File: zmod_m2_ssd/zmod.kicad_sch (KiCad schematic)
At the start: 16 parts, among them J1 MDT420M02001, J2 QTH-020-01-X-D-DP-A, U1 SN74LVC1T45DBV

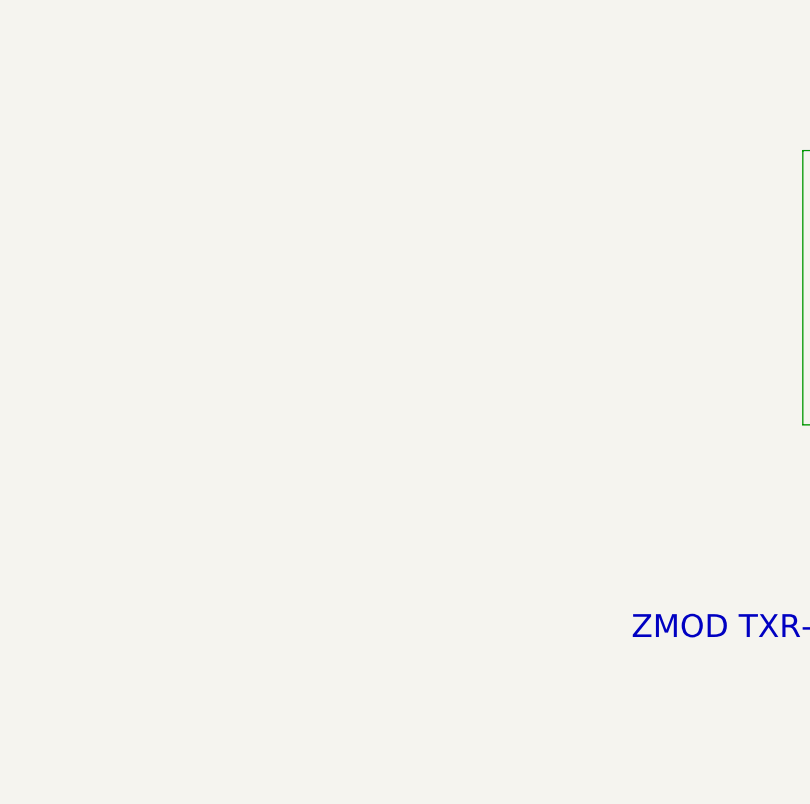
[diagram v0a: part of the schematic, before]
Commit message: adding clock chips for M.2
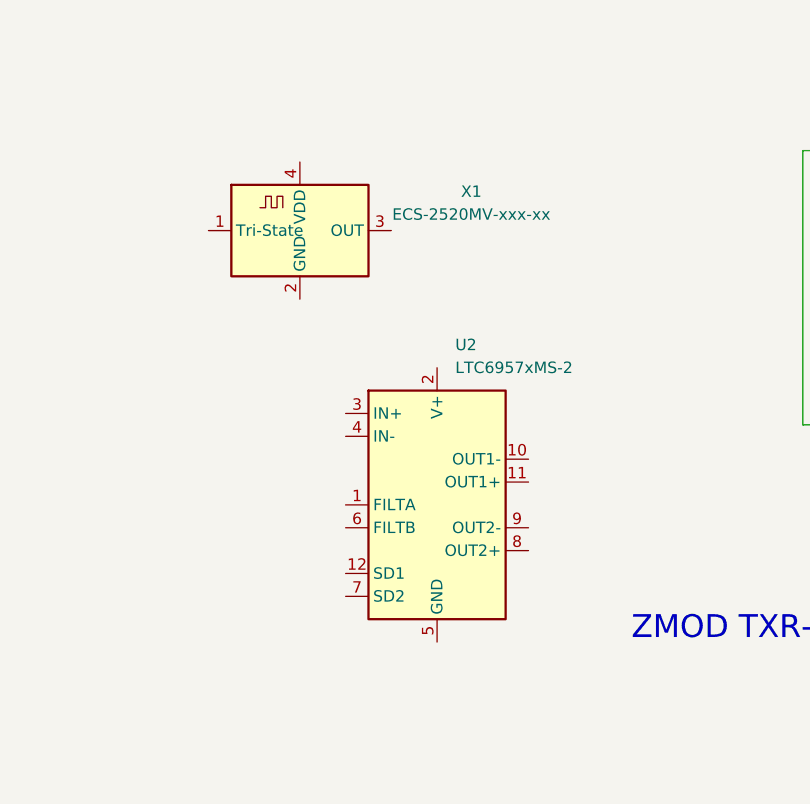
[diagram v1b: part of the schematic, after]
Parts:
- added U2: LTC6957xMS-2, Package_SO:MSOP-12_3x4mm_P0.65mm, symbol Interface:LTC6957xMS-2
- added X1: ECS-2520MV-xxx-xx, Oscillator:Oscillator_SMD_ECS_2520MV-xxx-xx-4Pin_2.5x2.0mm, symbol Oscillator:ECS-2520MV-xxx-xx
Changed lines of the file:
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@@
     (pin "9")
   )
-  (symbol (lib_id "power:+5V") (at 83.82 57.15 0) (unit 1)
-    (in_bom yes) (on_board yes) (fields_autoplaced)
-    (property "Reference" "#PWR02" (id 0) (at 83.82 60.96 0)
-      (effects (font (size 1.27 1.27)) hide)
-    )
-    (property "Value" "+5V" (id 1) (at 83.82 52.07 0))
-    (property "Footprint" "" (id 2) (at 83.82 57.15 0)
-      (effects (font (size 1.27 1.27)) hide)
-    )
-    (property "Datasheet" "" (id 3) (at 83.82 57.15 0)
-      (effects (font (size 1.27 1.27)) hide)
-    )
-    (pin "1")
-  )
-  (symbol (lib_id "power:+3V3") (at 269.24 72.39 0) (unit 1)
-    (in_bom yes) (on_board yes)
-    (property "Reference" "#PWR010" (id 0) (at 269.24 76.2 0)
-      (effects (font (size 1.27 1.27)) hide)
-    )
-    (property "Value" "+3V3" (id 1) (at 270.51 71.12 0)
-      (effects (font (size 1.27 1.27)) (justify left))
-    )
-    (property "Footprint" "" (id 2) (at 269.24 72.39 0)
-      (effects (font (size 1.27 1.27)) hide)
-    )
-    (property "Datasheet" "" (id 3) (at 269.24 72.39 0)
-      (effects (font (size 1.27 1.27)) hide)
-    )
-    (pin "1")
-  )
-  (symbol (lib_id "power:GND") (at 82.55 146.05 0) (unit 1)
-    (in_bom yes) (on_board yes) (fields_autoplaced)
-    (property "Reference" "#PWR0101" (id 0) (at 82.55 152.4 0)
-      (effects (font (size 1.27 1.27)) hide)
-    )
-    (property "Value" "GND" (id 1) (at 82.55 151.13 0))
-    (property "Footprint" "" (id 2) (at 82.55 146.05 0)
-      (effects (font (size 1.27 1.27)) hide)
-    )
-    (property "Datasheet" "" (id 3) (at 82.55 146.05 0)
-      (effects (font (size 1.27 1.27)) hide)
-    )
-    (pin "1")
-  )
-  (symbol (lib_id "Mechanical:MountingHole_Pad") (at 38.1 191.77 0) (unit 1)
-    (in_bom yes) (on_board yes) (fields_autoplaced)
-    (property "Reference" "H3" (id 0) (at 40.64 189.2299 0)
-      (effects (font (size 1.27 1.27)) (justify left))
-    )
-    (property "Value" "MountingHole_Pad" (id 1) (at 40.64 191.7699 0)
-      (effects (font (size 1.27 1.27)) (justify left) hide)
-    )
-    (property "Footprint" "MountingHole:MountingHole_3.2mm_M3_DIN965_Pad_TopBottom" (id 2) (at 38.1 191.77 0)
-      (effects (font (size 1.27 1.27)) hide)
-    )
-    (property "Datasheet" "~" (id 3) (at 38.1 191.77 0)
-      (effects (font (size 1.27 1.27)) hide)
-    )
-    (pin "1")
-  )
-  (symbol (lib_id "Logic_LevelTranslator:SN74LVC1T45DBV") (at 146.05 50.8 0) (mirror y) (unit 1)
-    (in_bom yes) (on_board yes) (fields_autoplaced)
-    (property "Reference" "U1" (id 0) (at 128.27 46.4693 0))
-    (property "Value" "SN74LVC1T45DBV" (id 1) (at 128.27 49.0093 0))
-    (property "Footprint" "Package_TO_SOT_SMD:SOT-23-6" (id 2) (at 146.05 62.23 0)
-      (effects (font (size 1.27 1.27)) hide)
-    )
-    (property "Datasheet" "http://www.ti.com/lit/ds/symlink/sn74lvc1t45.pdf" (id 3) (at 168.91 67.31 0)
-      (effects (font (size 1.27 1.27)) hide)
-    )
-    (pin "1")
+  (symbol (lib_id "Interface:LTC6957xMS-2") (at 162.56 156.21 0) (unit 1)
+    (in_bom yes) (on_board yes) (fields_autoplaced)
+    (property "Reference" "U2" (id 0) (at 164.5794 138.43 0)
+      (effects (font (size 1.27 1.27)) (justify left))
+    )
+    (property "Value" "LTC6957xMS-2" (id 1) (at 164.5794 140.97 0)
+      (effects (font (size 1.27 1.27)) (justify left))
+    )
+    (property "Footprint" "Package_SO:MSOP-12_3x4mm_P0.65mm" (id 2) (at 162.56 172.72 0)
+      (effects (font (size 1.27 1.27)) hide)
+    )
+    (property "Datasheet" "https://www.analog.com/media/en/technical-documentation/data-sheets/6957fb.pdf" (id 3) (at 162.56 156.21 0)
+      (effects (font (size 1.27 1.27)) hide)
+    )
+    (pin "1")
+    (pin "10")
+    (pin "11")
+    (pin "12")
     (pin "2")
     (pin "3")
@@
     (pin "5")
     (pin "6")
+    (pin "7")
+    (pin "8")
+    (pin "9")
+  )
+  (symbol (lib_id "power:+5V") (at 83.82 57.15 0) (unit 1)
+    (in_bom yes) (on_board yes) (fields_autoplaced)
+    (property "Reference" "#PWR02" (id 0) (at 83.82 60.96 0)
+      (effects (font (size 1.27 1.27)) hide)
+    )
+    (property "Value" "+5V" (id 1) (at 83.82 52.07 0))
+    (property "Footprint" "" (id 2) (at 83.82 57.15 0)
+      (effects (font (size 1.27 1.27)) hide)
+    )
+    (property "Datasheet" "" (id 3) (at 83.82 57.15 0)
+      (effects (font (size 1.27 1.27)) hide)
+    )
+    (pin "1")
+  )
+  (symbol (lib_id "Oscillator:ECS-2520MV-xxx-xx") (at 147.32 125.73 0) (unit 1)
+    (in_bom yes) (on_board yes) (fields_autoplaced)
+    (property "Reference" "X1" (id 0) (at 166.37 121.3993 0))
+    (property "Value" "ECS-2520MV-xxx-xx" (id 1) (at 166.37 123.9393 0))
+    (property "Footprint" "Oscillator:Oscillator_SMD_ECS_2520MV-xxx-xx-4Pin_2.5x2.0mm" (id 2) (at 158.75 134.62 0)
+      (effects (font (size 1.27 1.27)) hide)
+    )
+    (property "Datasheet" "https://www.ecsxtal.com/store/pdf/ECS-2520MV.pdf" (id 3) (at 142.875 122.555 0)
+      (effects (font (size 1.27 1.27)) hide)
+    )
+    (pin "1")
+    (pin "2")
+    (pin "3")
+    (pin "4")
+  )
+  (symbol (lib_id "power:+3V3") (at 269.24 72.39 0) (unit 1)
+    (in_bom yes) (on_board yes)
+    (property "Reference" "#PWR010" (id 0) (at 269.24 76.2 0)
+      (effects (font (size 1.27 1.27)) hide)
+    )
+    (property "Value" "+3V3" (id 1) (at 270.51 71.12 0)
+      (effects (font (size 1.27 1.27)) (justify left))
+    )
+    (property "Footprint" "" (id 2) (at 269.24 72.39 0)
+      (effects (font (size 1.27 1.27)) hide)
+    )
+    (property "Datasheet" "" (id 3) (at 269.24 72.39 0)
+      (effects (font (size 1.27 1.27)) hide)
+    )
+    (pin "1")
+  )
+  (symbol (lib_id "power:GND") (at 82.55 146.05 0) (unit 1)
+    (in_bom yes) (on_board yes) (fields_autoplaced)
+    (property "Reference" "#PWR0101" (id 0) (at 82.55 152.4 0)
+      (effects (font (size 1.27 1.27)) hide)
+    )
+    (property "Value" "GND" (id 1) (at 82.55 151.13 0))
+    (property "Footprint" "" (id 2) (at 82.55 146.05 0)
+      (effects (font (size 1.27 1.27)) hide)
+    )
+    (property "Datasheet" "" (id 3) (at 82.55 146.05 0)
+      (effects (font (size 1.27 1.27)) hide)
+    )
+    (pin "1")
+  )
+  (symbol (lib_id "Mechanical:MountingHole_Pad") (at 38.1 191.77 0) (unit 1)
+    (in_bom yes) (on_board yes) (fields_autoplaced)
+    (property "Reference" "H3" (id 0) (at 40.64 189.2299 0)
+      (effects (font (size 1.27 1.27)) (justify left))
+    )
+    (property "Value" "MountingHole_Pad" (id 1) (at 40.64 191.7699 0)
+      (effects (font (size 1.27 1.27)) (justify left) hide)
+    )
+    (property "Footprint" "MountingHole:MountingHole_3.2mm_M3_DIN965_Pad_TopBottom" (id 2) (at 38.1 191.77 0)
+      (effects (font (size 1.27 1.27)) hide)
+    )
+    (property "Datasheet" "~" (id 3) (at 38.1 191.77 0)
+      (effects (font (size 1.27 1.27)) hide)
+    )
+    (pin "1")
+  )
+  (symbol (lib_id "Logic_LevelTranslator:SN74LVC1T45DBV") (at 146.05 50.8 0) (mirror y) (unit 1)
+    (in_bom yes) (on_board yes) (fields_autoplaced)
+    (property "Reference" "U1" (id 0) (at 128.27 46.4693 0))
+    (property "Value" "SN74LVC1T45DBV" (id 1) (at 128.27 49.0093 0))
+    (property "Footprint" "Package_TO_SOT_SMD:SOT-23-6" (id 2) (at 146.05 62.23 0)
+      (effects (font (size 1.27 1.27)) hide)
+    )
+    (property "Datasheet" "http://www.ti.com/lit/ds/symlink/sn74lvc1t45.pdf" (id 3) (at 168.91 67.31 0)
+      (effects (font (size 1.27 1.27)) hide)
+    )
+    (pin "1")
+    (pin "2")
+    (pin "3")
+    (pin "4")
+    (pin "5")
+    (pin "6")
   )
   (symbol (lib_id "power:GND") (at 238.76 151.13 0) (unit 1)
@@
       (reference "U1") (unit 1) (value "SN74LVC1T45DBV") (footprint "Package_TO_SOT_SMD:SOT-23-6")
     )
-  )
+    (path "/73d9a73e-e38d-4675-ba62-7d628305395e"
+      (reference "U2") (unit 1) (value "LTC6957xMS-2") (footprint "Package_SO:MSOP-12_3x4mm_P0.65mm")
+    )
+    (path "/7c512e96-8c27-4e61-97e0-2f602c82f7f4"
+      (reference "X1") (unit 1) (value "ECS-2520MV-xxx-xx") (footprint "Oscillator:Oscillator_SMD_ECS_2520MV-xxx-xx-4Pin_2.5x2.0mm")
+    )
+  )

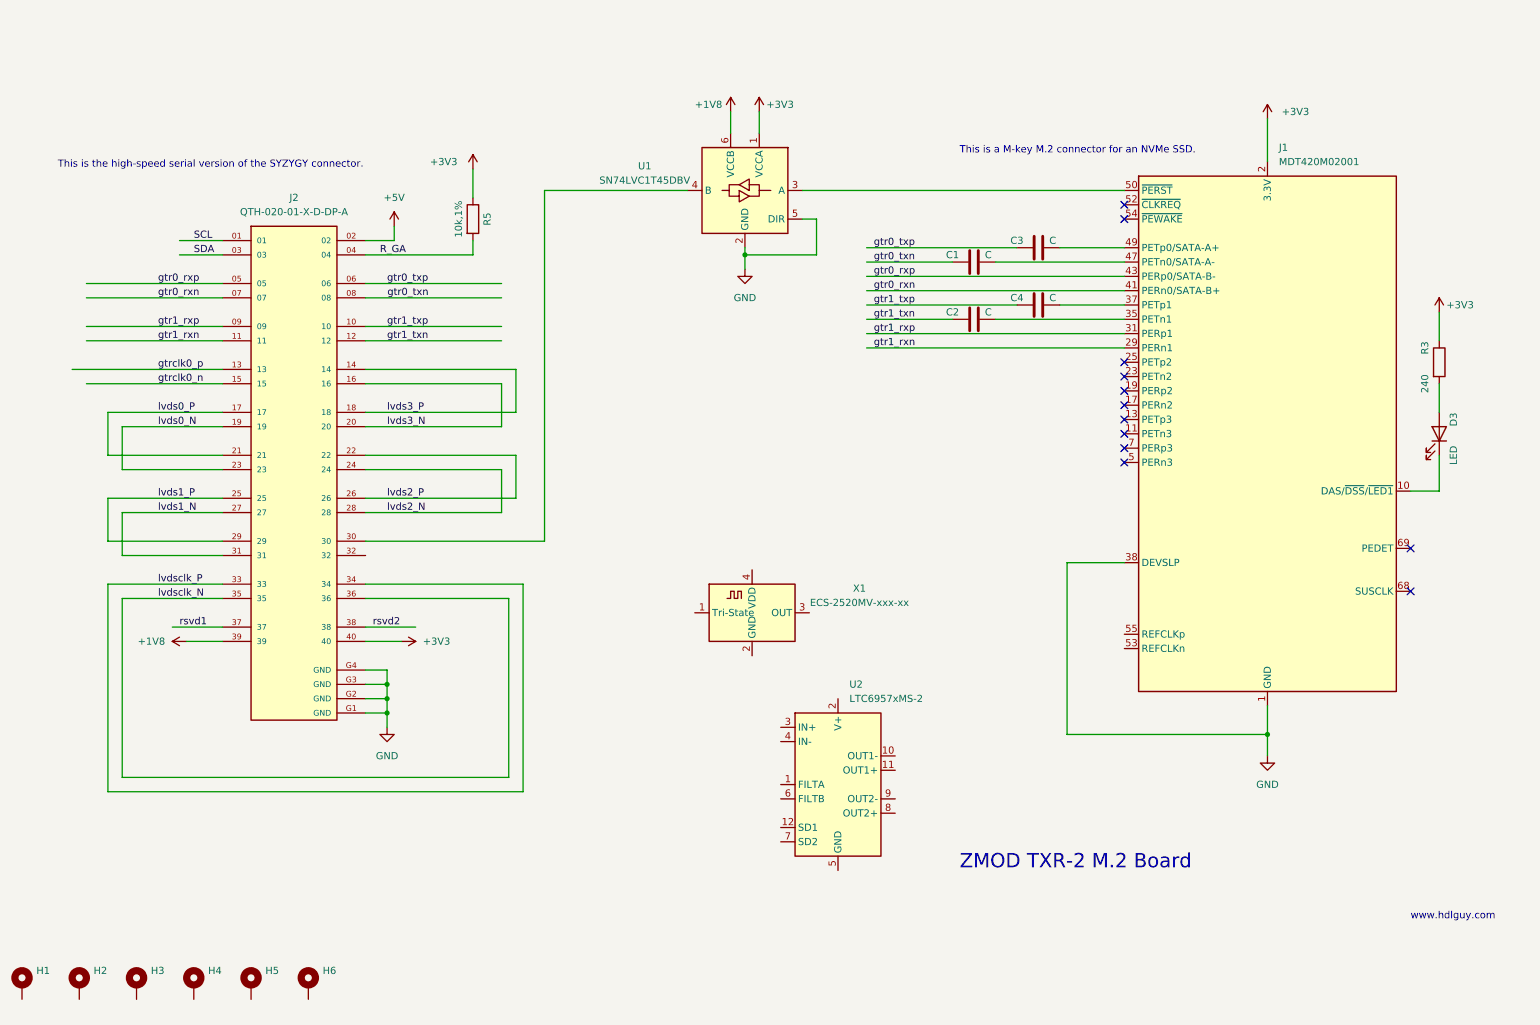
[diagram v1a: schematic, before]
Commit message: added referenc oscillator and clock buffer.
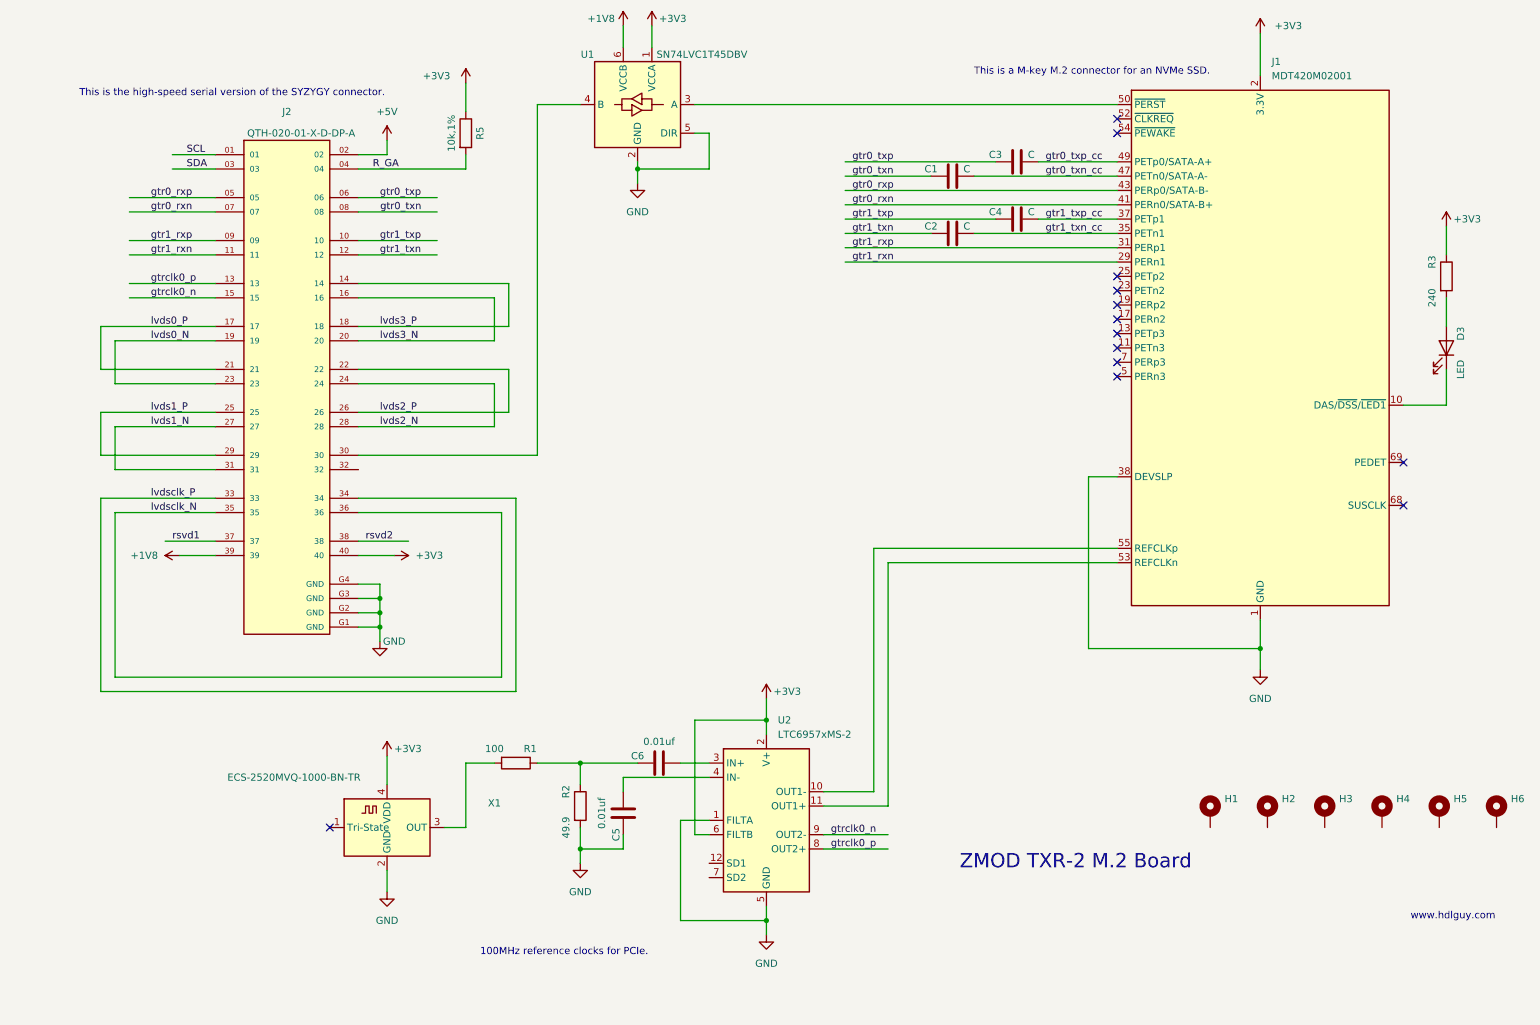
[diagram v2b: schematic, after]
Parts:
- added C5, C6: 0.01uf, Capacitor_SMD:C_0603_1608Metric, symbol Device:C
- added R1: 100, Resistor_SMD:R_0603_1608Metric, symbol Device:R
- added R2: 49.9, Resistor_SMD:R_0603_1608Metric, symbol Device:R
- X1: value ECS-2520MV-xxx-xx -> ECS-2520MVQ-1000-BN-TR
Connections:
- net +3V3: now also U2.2 (V+), U2.6 (FILTB), X1.4 (VDD)
- net GND: now also U2.1 (FILTA), U2.5 (GND), X1.2 (GND), C5.1, R2.2
- net gtrclk0_n: now also U2.9 (OUT2-)
- net gtrclk0_p: now also U2.8 (OUT2+)
- net gtr0_txn_cc: now reaches C1.2, J1.47 (PETn0/SATA-A-)
- net gtr1_txn_cc: now reaches C2.2, J1.35 (PETn1)
- net gtr1_txp_cc: now reaches C4.2, J1.37 (PETp1)
- net gtr0_txp_cc: now reaches C3.2, J1.49 (PETp0/SATA-A+)
- net at J1.53 (REFCLKn): now also U2.11 (OUT1+)
- net at J1.55 (REFCLKp): now also U2.10 (OUT1-)
- net at U2.3 (IN+): now also C6.2
- net at U2.4 (IN-): now also C5.2
- net at X1.3 (OUT): now also R1.2
- new net: C6.1, R1.1, R2.1
- no-connect marks 12 -> 13
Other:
- note added: "100MHz reference clocks for PCIe."
- moved on the sheet: C1, C2, C3, C4, D3, H1, H2, H3, H4, H5, H6, J1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

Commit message: placed all components and locked down mounting holes and connectors, need M.2 screw hole
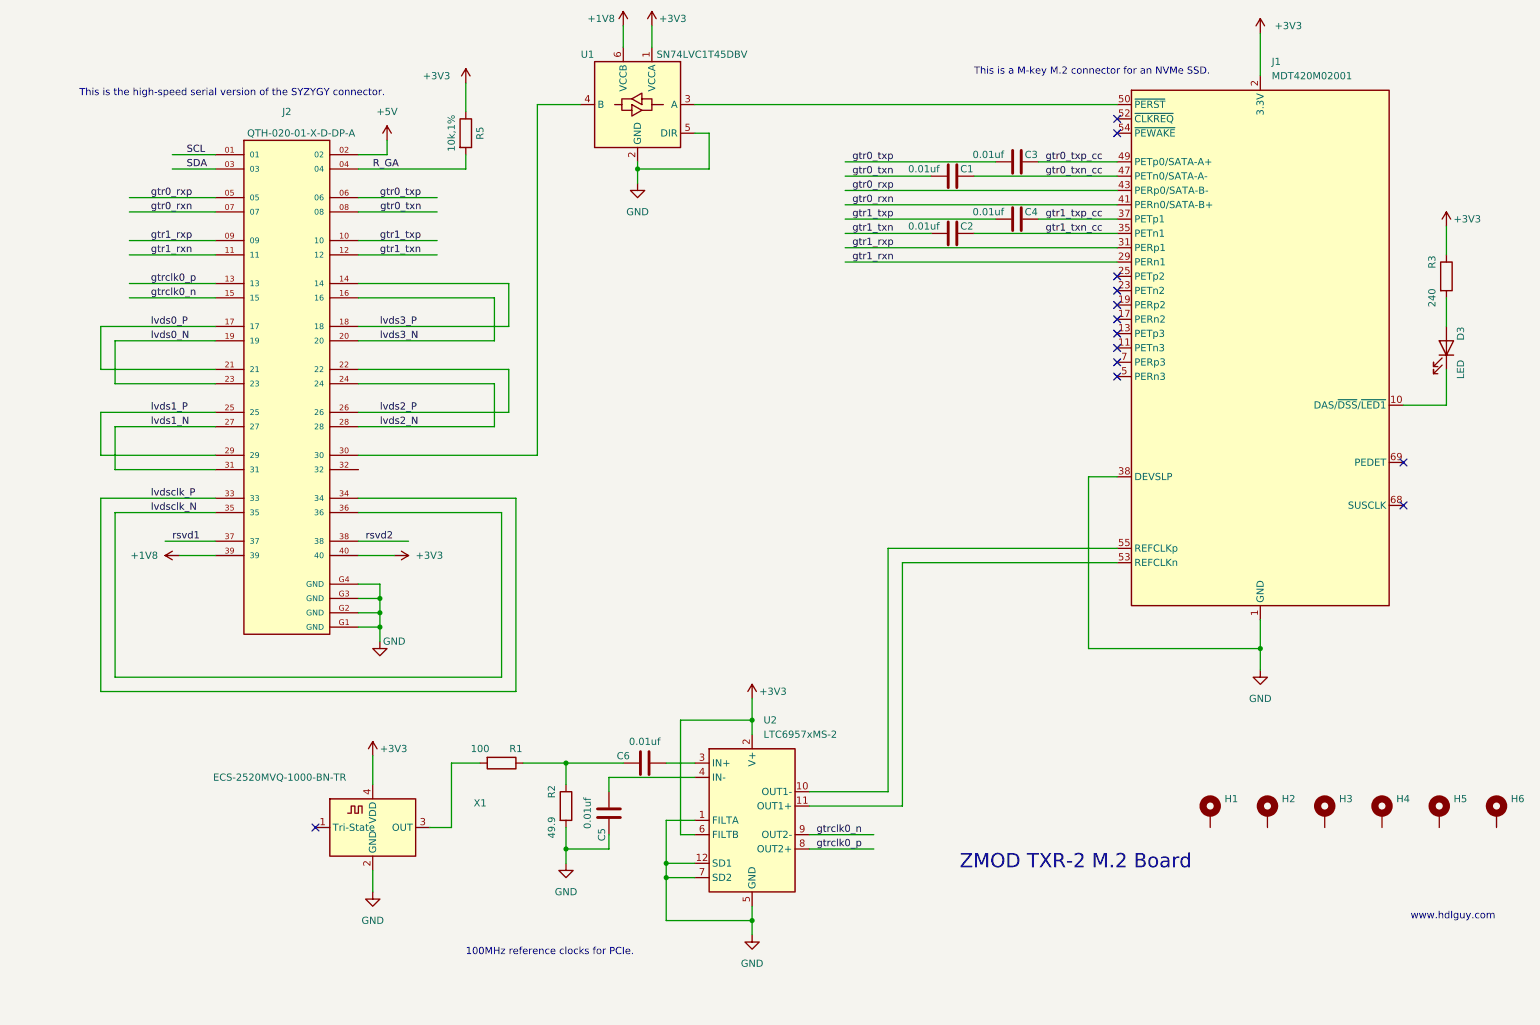
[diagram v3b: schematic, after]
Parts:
- C1, C2, C3, C4: value C -> 0.01uf
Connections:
- net GND: now also U2.12 (SD1), U2.7 (SD2)
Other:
- moved on the sheet: C5, C6, R1, R2, U2, X1
